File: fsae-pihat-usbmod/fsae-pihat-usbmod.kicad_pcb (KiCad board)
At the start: 2 copper layers, 41.9 x 18.2 mm, 3 parts, among them J1 Conn_01x03_Socket, J2 PDC004 V2 PD Trigger, U1 MT3608 Boost

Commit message: feat: readme, journal, pcb updates
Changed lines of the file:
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@@
 	)
 	(segment
-		(start 130.15 92.7)
-		(end 110.515 92.7)
-		(width 0.5)
+		(start 129.385 92.715)
+		(end 132.15 89.95)
+		(width 0.75)
 		(layer "B.Cu")
 		(net 2)
 	)
 	(segment
-		(start 132.9 89.95)
-		(end 130.15 92.7)
-		(width 0.5)
+		(start 110.5 92.715)
+		(end 129.385 92.715)
+		(width 0.75)
 		(layer "B.Cu")
 		(net 2)
 	)
 	(segment
-		(start 110.515 92.7)
-		(end 110.5 92.715)
-		(width 0.5)
+		(start 132.15 89.95)
+		(end 132.9 89.95)
+		(width 0.75)
 		(layer "B.Cu")
 		(net 2)

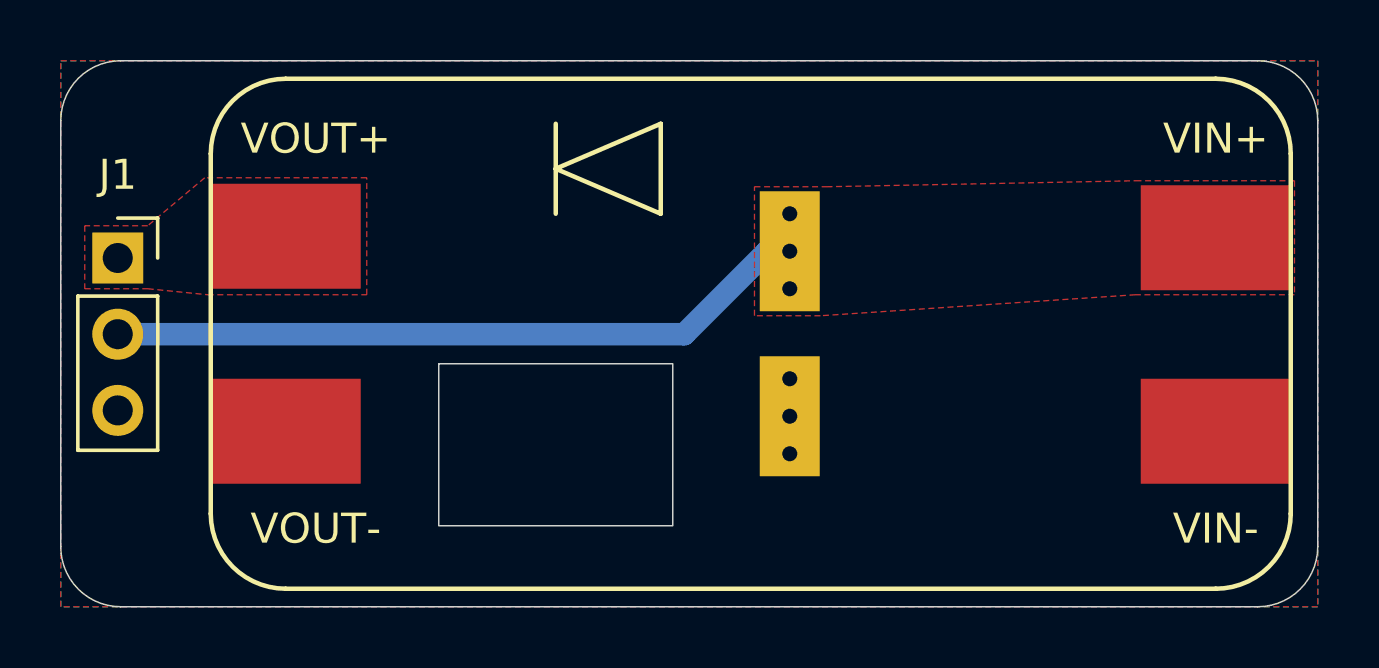
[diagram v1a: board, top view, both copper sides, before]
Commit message: fix: missed hat pullup; feat: new pd module
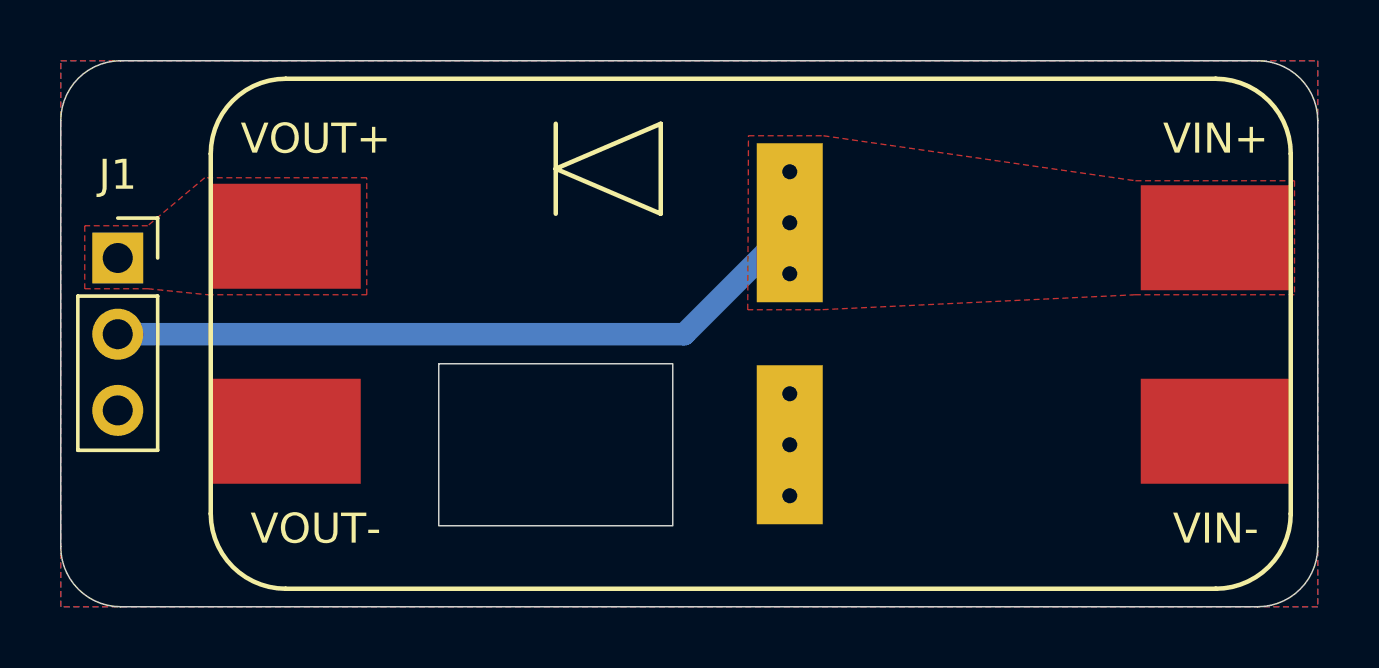
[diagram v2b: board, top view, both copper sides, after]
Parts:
- J2: value PDC004 V2 PD Trigger -> HUSB238 Module; footprint custom:PDC004-Footprint -> custom:HUSB238_module_purple
- moved J2 2.05 mm to (142.8, 92.7)
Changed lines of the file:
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@@
 		(property ki_fp_filters "Connector*:*_1x??_*")
 		(sheetname "/")
-		(sheetfile "f1-pihat-module.kicad_sch")
+		(sheetfile "fsae-pihat-usbmod.kicad_sch")
 		(attr through_hole)
 		(fp_line
@@
 		)
 		(sheetname "/")
-		(sheetfile "f1-pihat-module.kicad_sch")
+		(sheetfile "fsae-pihat-usbmod.kicad_sch")
 		(attr through_hole)
 		(fp_line
@@
 		)
 	)
-	(footprint "custom:PDC004-Footprint"
+	(footprint "custom:HUSB238_module_purple"
 		(layer "B.Cu")
-		(at 140.7 92.7 -90)
+		(at 142.75 92.7 -90)
 		(property "Reference" "J2"
-			(at 0 10.427 90)
+			(at 0 11.927 90)
 			(layer "B.SilkS")
 			(effects
@@
 			)
 		)
-		(property "Value" "PDC004 V2 PD Trigger"
+		(property "Value" "HUSB238 Module"
 			(at 0 -10.427 90)
 			(layer "B.Fab")
@@
 		)
 		(property "Min Supply Voltage" ""
-			(at 0 0 270)
+			(at 0 0 90)
 			(unlocked yes)
 			(layer "B.Fab")
@@
 		)
 		(property "Output Current" ""
-			(at 0 0 270)
+			(at 0 0 90)
 			(unlocked yes)
 			(layer "B.Fab")
@@
 		)
 		(property "Max Supply Voltage" ""
-			(at 0 0 270)
+			(at 0 0 90)
 			(unlocked yes)
 			(layer "B.Fab")
@@
 		)
 		(property "Pins" ""
-			(at 0 0 270)
+			(at 0 0 90)
 			(unlocked yes)
 			(layer "B.Fab")
@@
 		)
 		(property "Max Power Dissipation" ""
-			(at 0 0 270)
+			(at 0 0 90)
 			(unlocked yes)
 			(layer "B.Fab")
@@
 		)
 		(property "Max Operating Temperature" ""
-			(at 0 0 270)
+			(at 0 0 90)
 			(unlocked yes)
 			(layer "B.Fab")
@@
 		)
 		(property "Dropout Voltage" ""
-			(at 0 0 270)
+			(at 0 0 90)
 			(unlocked yes)
 			(layer "B.Fab")
@@
 		)
 		(property "Nominal Supply Current" ""
-			(at 0 0 270)
+			(at 0 0 90)
 			(unlocked yes)
 			(layer "B.Fab")
@@
 		)
 		(property "Case/Package" ""
-			(at 0 0 270)
+			(at 0 0 90)
 			(unlocked yes)
 			(layer "B.Fab")
@@
 		)
 		(property "Frequency" ""
-			(at 0 0 270)
+			(at 0 0 90)
 			(unlocked yes)
 			(layer "B.Fab")
@@
 		)
 		(property "Output Voltage" ""
-			(at 0 0 270)
+			(at 0 0 90)
 			(unlocked yes)
 			(layer "B.Fab")
@@
 		)
 		(property "Mounting Technology" ""
-			(at 0 0 270)
+			(at 0 0 90)
 			(unlocked yes)
 			(layer "B.Fab")
@@
 		)
 		(property "RoHS Compliant" ""
-			(at 0 0 270)
+			(at 0 0 90)
 			(unlocked yes)
 			(layer "B.Fab")
@@
 		)
 		(property "Min Operating Temperature" ""
-			(at 0 0 270)
-			(unlocked yes)
-			(layer "B.Fab")
-			(hide yes)
-			(effects
-				(font
-					(size 1 1)
-					(thickness 0.15)
-				)
-				(justify mirror)
-			)
-		)
-		(property ki_fp_filters "*PDC004-Footprint*")
+			(at 0 0 90)
+			(unlocked yes)
+			(layer "B.Fab")
+			(hide yes)
+			(effects
+				(font
+					(size 1 1)
+					(thickness 0.15)
+				)
+				(justify mirror)
+			)
+		)
+		(property ki_fp_filters "*HUSB238_module*")
 		(sheetname "/")
-		(sheetfile "f1-pihat-module.kicad_sch")
-		(fp_line
-			(start -5.35 9.4)
-			(end 5.35 9.4)
-			(stroke
-				(width 0.5)
+		(sheetfile "fsae-pihat-usbmod.kicad_sch")
+		(fp_line
+			(start -6.7 11.3)
+			(end 6.7 11.3)
+			(stroke
+				(width 0.4)
 				(type solid)
 			)
@@
 		)
 		(fp_line
-			(start -5.35 -9.4)
-			(end -5.35 9.4)
-			(stroke
-				(width 0.5)
+			(start -6.7 -11.3)
+			(end -6.7 11.3)
+			(stroke
+				(width 0.4)
 				(type solid)
 			)
@@
 		)
 		(fp_line
-			(start -5.35 -9.4)
-			(end 5.35 -9.4)
-			(stroke
-				(width 0.5)
+			(start -6.7 -11.3)
+			(end 6.7 -11.3)
+			(stroke
+				(width 0.4)
 				(type solid)
 			)
@@
 		)
 		(fp_line
-			(start 5.35 -9.4)
-			(end 5.35 9.35)
-			(stroke
-				(width 0.5)
+			(start 6.7 -11.3)
+			(end 6.7 11.3)
+			(stroke
+				(width 0.4)
 				(type solid)
 			)
@@
 		)
 		(fp_line
-			(start -5.55 9.6)
-			(end 5.55 9.6)
+			(start -6.5 11.1)
+			(end 6.5 11.1)
 			(stroke
 				(width 0.254)
@@
 		)
 		(fp_line
-			(start -5.55 -9.6)
-			(end -5.55 9.6)
+			(start -6.5 -11.1)
+			(end -6.5 11.1)
 			(stroke
 				(width 0.254)
@@
 		)
 		(fp_line
-			(start -5.55 -9.6)
-			(end 5.55 -9.6)
+			(start -6.5 -11.1)
+			(end 6.5 -11.1)
 			(stroke
 				(width 0.254)
@@
 		)
 		(fp_line
-			(start 5.55 -9.6)
-			(end 5.55 9.6)
+			(start 6.5 -11.1)
+			(end 6.5 11.1)
 			(stroke
 				(width 0.254)
@@
 		)
 		(pad "1" thru_hole circle
-			(at -4 7.8 270)
+			(at -5.4 9.85 270)
 			(size 0.7 0.7)
 			(drill 0.5)
@@
 		)
 		(pad "1" thru_hole rect
-			(at -2.75 7.8 270)
-			(size 4 2)
+			(at -3.7 9.85 270)
+			(size 5.3 2.2)
 			(drill 0.5)
 			(layers "*.Cu" "B.Mask")
@@
 		)
 		(pad "1" thru_hole circle
-			(at -1.5 7.8 270)
+			(at -2 9.85 270)
 			(size 0.7 0.7)
 			(drill 0.5)
@@
 		)
 		(pad "2" thru_hole circle
-			(at 1.5 7.8 270)
+			(at 2 9.85 270)
 			(size 0.7 0.7)
 			(drill 0.5)
@@
 		)
 		(pad "2" thru_hole rect
-			(at 2.75 7.8 270)
-			(size 4 2)
+			(at 3.7 9.85 270)
+			(size 5.3 2.2)
 			(drill 0.5)
 			(layers "*.Cu" "B.Mask")
@@
 		)
 		(pad "2" thru_hole circle
-			(at 4 7.8 270)
+			(at 5.4 9.85 270)
 			(size 0.7 0.7)
 			(drill 0.5)
@@
 		(polygon
 			(pts
-				(xy 131.724077 87.8) (xy 134.124077 87.8) (xy 144.424077 87.6) (xy 149.724077 87.6) (xy 149.724077 91.4)
-				(xy 144.424077 91.4) (xy 133.924077 92.1) (xy 131.724077 92.1)
-			)
-		)
+				(xy 131.524077 86.1) (xy 134.024077 86.1) (xy 144.424077 87.6) (xy 149.724077 87.6) (xy 149.724077 91.4)
+				(xy 144.424077 91.4) (xy 133.924077 91.9) (xy 131.5 91.9)
+			)
+		)
